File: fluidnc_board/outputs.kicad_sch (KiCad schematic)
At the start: 20 parts, among them J31 Screw_Terminal_01x02, J32 Screw_Terminal_01x02, J33 Screw_Terminal_01x02, J34 Screw_Terminal_01x02, Q11 IRF7809AVTRPBF, Q12 IRF7809AVTRPBF, Q13 IRF7809AVTRPBF, Q14 IRF7809AVTRPBF

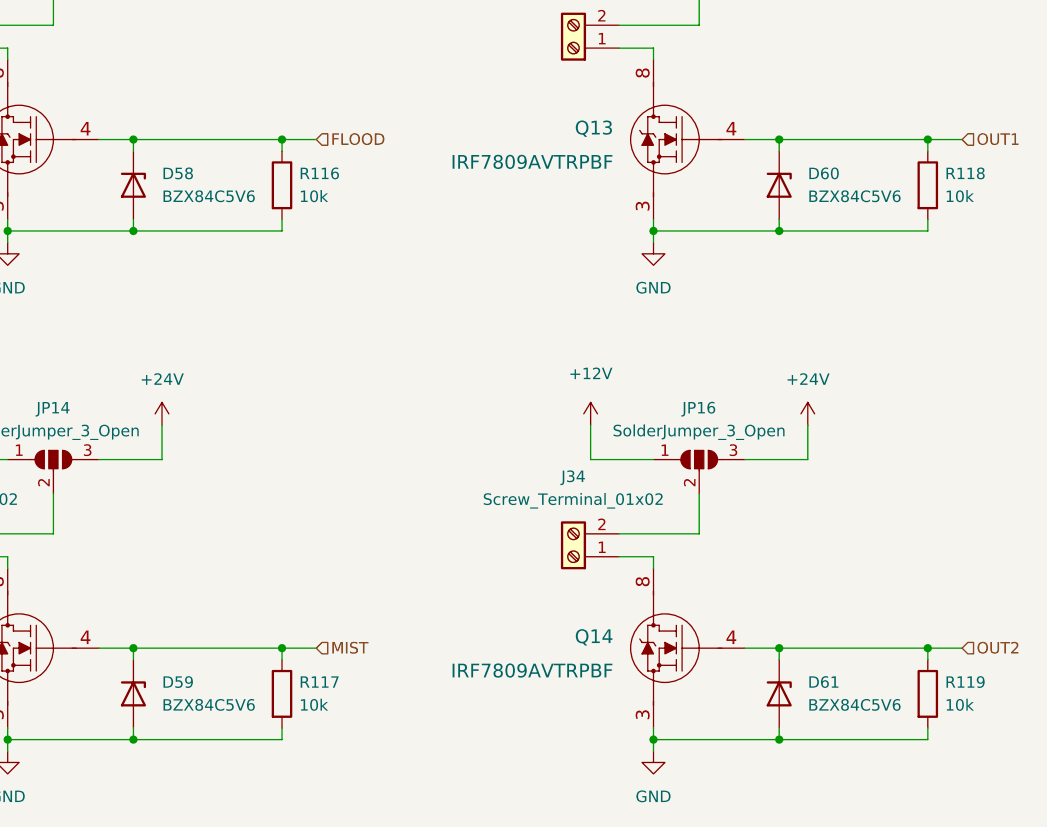
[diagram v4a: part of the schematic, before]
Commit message: one driver unit layout
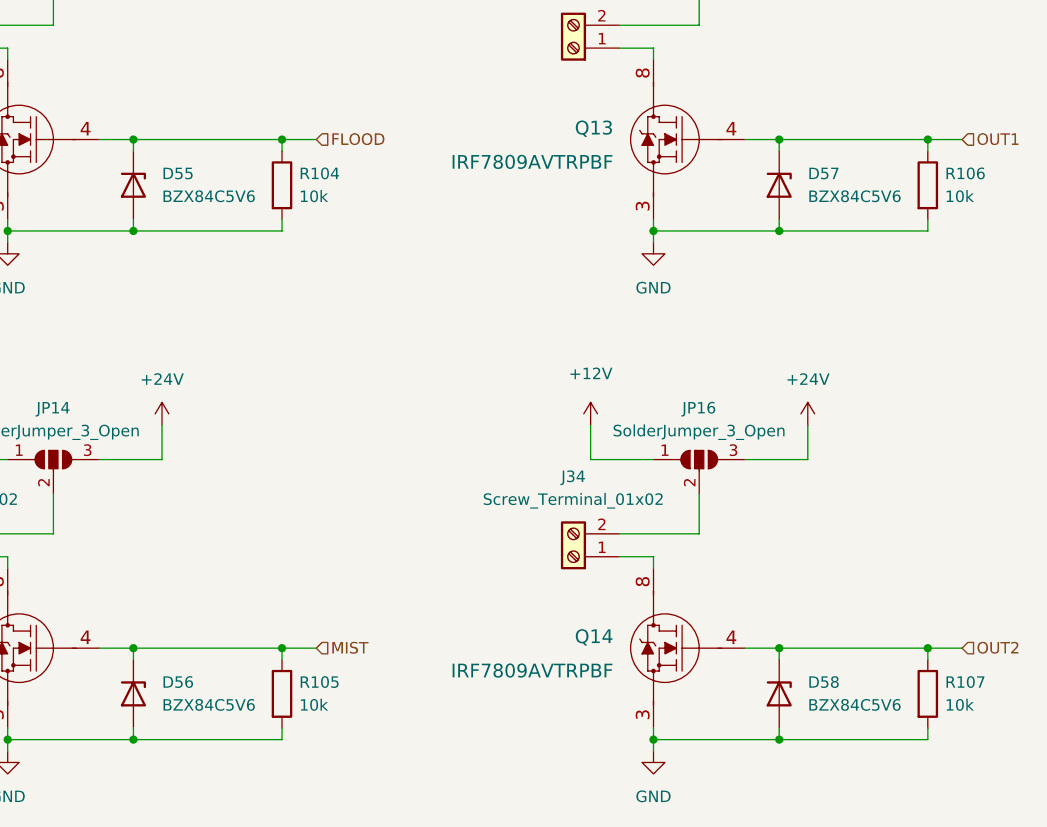
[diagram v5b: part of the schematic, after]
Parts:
- renumbered D58 to D55, D59 to D56, D60 to D57, D61 to D58, R116 to R104, R117 to R105, R118 to R106, R119 to R107
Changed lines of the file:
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@@
   (symbol (lib_id "power:GND") (at 178.435 87.63 0) (unit 1)
     (in_bom yes) (on_board yes) (fields_autoplaced)
-    (property "Reference" "#PWR0228" (id 0) (at 178.435 93.98 0)
+    (property "Reference" "#PWR0216" (id 0) (at 178.435 93.98 0)
       (effects (font (size 1.27 1.27)) hide)
     )
@@
   (symbol (lib_id "Diode:BZX84Cxx") (at 192.405 81.28 270) (unit 1)
     (in_bom yes) (on_board yes) (fields_autoplaced)
-    (property "Reference" "D60" (id 0) (at 195.58 80.0099 90)
+    (property "Reference" "D57" (id 0) (at 195.58 80.0099 90)
       (effects (font (size 1.27 1.27)) (justify left))
     )
@@
   (symbol (lib_id "Device:R") (at 137.16 81.28 0) (unit 1)
     (in_bom yes) (on_board yes) (fields_autoplaced)
-    (property "Reference" "R116" (id 0) (at 139.065 80.0099 0)
+    (property "Reference" "R104" (id 0) (at 139.065 80.0099 0)
       (effects (font (size 1.27 1.27)) (justify left))
     )
@@
   (symbol (lib_id "power:+24V") (at 123.825 51.435 0) (unit 1)
     (in_bom yes) (on_board yes) (fields_autoplaced)
-    (property "Reference" "#PWR0224" (id 0) (at 123.825 55.245 0)
+    (property "Reference" "#PWR0212" (id 0) (at 123.825 55.245 0)
       (effects (font (size 1.27 1.27)) hide)
     )
@@
   (symbol (lib_id "Diode:BZX84Cxx") (at 192.405 137.795 270) (unit 1)
     (in_bom yes) (on_board yes) (fields_autoplaced)
-    (property "Reference" "D61" (id 0) (at 195.58 136.5249 90)
+    (property "Reference" "D58" (id 0) (at 195.58 136.5249 90)
       (effects (font (size 1.27 1.27)) (justify left))
     )
@@
   (symbol (lib_id "power:+24V") (at 123.825 107.95 0) (unit 1)
     (in_bom yes) (on_board yes) (fields_autoplaced)
-    (property "Reference" "#PWR0225" (id 0) (at 123.825 111.76 0)
+    (property "Reference" "#PWR0213" (id 0) (at 123.825 111.76 0)
       (effects (font (size 1.27 1.27)) hide)
     )
@@
   (symbol (lib_id "Diode:BZX84Cxx") (at 120.65 81.28 270) (unit 1)
     (in_bom yes) (on_board yes) (fields_autoplaced)
-    (property "Reference" "D58" (id 0) (at 123.825 80.0099 90)
+    (property "Reference" "D55" (id 0) (at 123.825 80.0099 90)
       (effects (font (size 1.27 1.27)) (justify left))
     )
@@
   (symbol (lib_id "power:GND") (at 106.68 87.63 0) (unit 1)
     (in_bom yes) (on_board yes) (fields_autoplaced)
-    (property "Reference" "#PWR0222" (id 0) (at 106.68 93.98 0)
+    (property "Reference" "#PWR0210" (id 0) (at 106.68 93.98 0)
       (effects (font (size 1.27 1.27)) hide)
     )
@@
   (symbol (lib_id "power:+12V") (at 99.695 51.435 0) (unit 1)
     (in_bom yes) (on_board yes) (fields_autoplaced)
-    (property "Reference" "#PWR0220" (id 0) (at 99.695 55.245 0)
+    (property "Reference" "#PWR0208" (id 0) (at 99.695 55.245 0)
       (effects (font (size 1.27 1.27)) hide)
     )
@@
   (symbol (lib_id "power:+24V") (at 195.58 107.95 0) (unit 1)
     (in_bom yes) (on_board yes) (fields_autoplaced)
-    (property "Reference" "#PWR0231" (id 0) (at 195.58 111.76 0)
+    (property "Reference" "#PWR0219" (id 0) (at 195.58 111.76 0)
       (effects (font (size 1.27 1.27)) hide)
     )
@@
   (symbol (lib_id "Device:R") (at 208.915 137.795 0) (unit 1)
     (in_bom yes) (on_board yes) (fields_autoplaced)
-    (property "Reference" "R119" (id 0) (at 210.82 136.5249 0)
+    (property "Reference" "R107" (id 0) (at 210.82 136.5249 0)
       (effects (font (size 1.27 1.27)) (justify left))
     )
@@
   (symbol (lib_id "power:GND") (at 106.68 144.145 0) (unit 1)
     (in_bom yes) (on_board yes) (fields_autoplaced)
-    (property "Reference" "#PWR0223" (id 0) (at 106.68 150.495 0)
+    (property "Reference" "#PWR0211" (id 0) (at 106.68 150.495 0)
       (effects (font (size 1.27 1.27)) hide)
     )
@@
   (symbol (lib_id "power:+12V") (at 171.45 107.95 0) (unit 1)
     (in_bom yes) (on_board yes) (fields_autoplaced)
-    (property "Reference" "#PWR0227" (id 0) (at 171.45 111.76 0)
+    (property "Reference" "#PWR0215" (id 0) (at 171.45 111.76 0)
       (effects (font (size 1.27 1.27)) hide)
     )
@@
   (symbol (lib_id "power:GND") (at 178.435 144.145 0) (unit 1)
     (in_bom yes) (on_board yes) (fields_autoplaced)
-    (property "Reference" "#PWR0229" (id 0) (at 178.435 150.495 0)
+    (property "Reference" "#PWR0217" (id 0) (at 178.435 150.495 0)
       (effects (font (size 1.27 1.27)) hide)
     )
@@
   (symbol (lib_id "Device:R") (at 208.915 81.28 0) (unit 1)
     (in_bom yes) (on_board yes) (fields_autoplaced)
-    (property "Reference" "R118" (id 0) (at 210.82 80.0099 0)
+    (property "Reference" "R106" (id 0) (at 210.82 80.0099 0)
       (effects (font (size 1.27 1.27)) (justify left))
     )
@@
   (symbol (lib_id "Device:R") (at 137.16 137.795 0) (unit 1)
     (in_bom yes) (on_board yes) (fields_autoplaced)
-    (property "Reference" "R117" (id 0) (at 139.065 136.5249 0)
+    (property "Reference" "R105" (id 0) (at 139.065 136.5249 0)
       (effects (font (size 1.27 1.27)) (justify left))
     )
@@
   (symbol (lib_id "power:+12V") (at 171.45 51.435 0) (unit 1)
     (in_bom yes) (on_board yes) (fields_autoplaced)
-    (property "Reference" "#PWR0226" (id 0) (at 171.45 55.245 0)
+    (property "Reference" "#PWR0214" (id 0) (at 171.45 55.245 0)
       (effects (font (size 1.27 1.27)) hide)
     )
@@
   (symbol (lib_id "power:+12V") (at 99.695 107.95 0) (unit 1)
     (in_bom yes) (on_board yes) (fields_autoplaced)
-    (property "Reference" "#PWR0221" (id 0) (at 99.695 111.76 0)
+    (property "Reference" "#PWR0209" (id 0) (at 99.695 111.76 0)
       (effects (font (size 1.27 1.27)) hide)
     )
@@
   (symbol (lib_id "Diode:BZX84Cxx") (at 120.65 137.795 270) (unit 1)
     (in_bom yes) (on_board yes) (fields_autoplaced)
-    (property "Reference" "D59" (id 0) (at 123.825 136.5249 90)
+    (property "Reference" "D56" (id 0) (at 123.825 136.5249 90)
       (effects (font (size 1.27 1.27)) (justify left))
     )
@@
   (symbol (lib_id "power:+24V") (at 195.58 51.435 0) (unit 1)
     (in_bom yes) (on_board yes) (fields_autoplaced)
-    (property "Reference" "#PWR0230" (id 0) (at 195.58 55.245 0)
-      (effects (font (size 1.27 1.27)) hide)
-    )
+    (property "Reference" "#PWR0218" (id 0) (at 195.58 55.245 0)
+      (effects (font (size 1.27 1.27)) hide)
+    )
